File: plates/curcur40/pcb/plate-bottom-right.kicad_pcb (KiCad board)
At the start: 2 copper layers, 116.1 x 88.3 mm, 0 parts

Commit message: move trackball
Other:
- board size 116.1 x 88.3 mm -> 125.6 x 88.3 mm
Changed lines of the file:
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@@
   )
   (net 0 "")
-  (gr_arc (start 119.970400 40.381250) (mid 119.677507 41.088357) (end 118.970400 41.381250) (stroke (width 0.2) (type solid)) (layer "Edge.Cuts"))
-  (gr_line (start 118.970400 41.381250) (end 82.862500 41.381250) (stroke (width 0.2) (type solid)) (layer "Edge.Cuts"))
-  (gr_line (start 82.862500 41.381250) (end 82.862500 62.562500) (stroke (width 0.2) (type solid)) (layer "Edge.Cuts"))
-  (gr_arc (start 82.862500 62.562500) (mid 82.569607 63.269607) (end 81.862500 63.562500) (stroke (width 0.2) (type solid)) (layer "Edge.Cuts"))
-  (gr_line (start 81.862500 63.562500) (end 4.862500 63.562500) (stroke (width 0.2) (type solid)) (layer "Edge.Cuts"))
-  (gr_arc (start 4.862500 63.562500) (mid 4.155393 63.269607) (end 3.862500 62.562500) (stroke (width 0.2) (type solid)) (layer "Edge.Cuts"))
-  (gr_line (start 3.862500 62.562500) (end 3.862500 -16.568750) (stroke (width 0.2) (type solid)) (layer "Edge.Cuts"))
   (gr_arc (start 3.862500 -16.568750) (mid 4.155393 -17.275857) (end 4.862500 -17.568750) (stroke (width 0.2) (type solid)) (layer "Edge.Cuts"))
   (gr_line (start 4.862500 -17.568750) (end 22.928400 -17.568750) (stroke (width 0.2) (type solid)) (layer "Edge.Cuts"))
@@
   (gr_arc (start 118.970400 -17.568750) (mid 119.677507 -17.275857) (end 119.970400 -16.568750) (stroke (width 0.2) (type solid)) (layer "Edge.Cuts"))
   (gr_line (start 119.970400 -16.568750) (end 119.970400 40.381250) (stroke (width 0.2) (type solid)) (layer "Edge.Cuts"))
-  (gr_arc (start 12.450000 44.487500) (mid 12.742893 43.780393) (end 13.450000 43.487500) (stroke (width 0.2) (type solid)) (layer "Edge.Cuts"))
-  (gr_line (start 13.450000 43.487500) (end 20.650000 43.487500) (stroke (width 0.2) (type solid)) (layer "Edge.Cuts"))
-  (gr_arc (start 20.650000 43.487500) (mid 21.357107 43.780393) (end 21.650000 44.487500) (stroke (width 0.2) (type solid)) (layer "Edge.Cuts"))
-  (gr_line (start 21.650000 44.487500) (end 21.650000 60.287500) (stroke (width 0.2) (type solid)) (layer "Edge.Cuts"))
-  (gr_arc (start 21.650000 60.287500) (mid 21.357107 60.994607) (end 20.650000 61.287500) (stroke (width 0.2) (type solid)) (layer "Edge.Cuts"))
-  (gr_line (start 20.650000 61.287500) (end 13.450000 61.287500) (stroke (width 0.2) (type solid)) (layer "Edge.Cuts"))
-  (gr_arc (start 13.450000 61.287500) (mid 12.742893 60.994607) (end 12.450000 60.287500) (stroke (width 0.2) (type solid)) (layer "Edge.Cuts"))
-  (gr_line (start 12.450000 60.287500) (end 12.450000 44.487500) (stroke (width 0.2) (type solid)) (layer "Edge.Cuts"))
+  (gr_arc (start 119.970400 40.381250) (mid 119.677507 41.088357) (end 118.970400 41.381250) (stroke (width 0.2) (type solid)) (layer "Edge.Cuts"))
+  (gr_line (start 118.970400 41.381250) (end 82.862500 41.381250) (stroke (width 0.2) (type solid)) (layer "Edge.Cuts"))
+  (gr_line (start 82.862500 41.381250) (end 82.862500 62.562500) (stroke (width 0.2) (type solid)) (layer "Edge.Cuts"))
+  (gr_arc (start 82.862500 62.562500) (mid 82.569607 63.269607) (end 81.862500 63.562500) (stroke (width 0.2) (type solid)) (layer "Edge.Cuts"))
+  (gr_line (start 81.862500 63.562500) (end -4.662500 63.562500) (stroke (width 0.2) (type solid)) (layer "Edge.Cuts"))
+  (gr_arc (start -4.662500 63.562500) (mid -5.369607 63.269607) (end -5.662500 62.562500) (stroke (width 0.2) (type solid)) (layer "Edge.Cuts"))
+  (gr_line (start -5.662500 62.562500) (end -5.662500 38.400000) (stroke (width 0.2) (type solid)) (layer "Edge.Cuts"))
+  (gr_arc (start -5.662500 38.400000) (mid -5.369607 37.692893) (end -4.662500 37.400000) (stroke (width 0.2) (type solid)) (layer "Edge.Cuts"))
+  (gr_line (start -4.662500 37.400000) (end 3.862500 37.400000) (stroke (width 0.2) (type solid)) (layer "Edge.Cuts"))
+  (gr_line (start 3.862500 37.400000) (end 3.862500 -16.568750) (stroke (width 0.2) (type solid)) (layer "Edge.Cuts"))
+  (gr_arc (start 2.925000 44.487500) (mid 3.217893 43.780393) (end 3.925000 43.487500) (stroke (width 0.2) (type solid)) (layer "Edge.Cuts"))
+  (gr_line (start 3.925000 43.487500) (end 11.125000 43.487500) (stroke (width 0.2) (type solid)) (layer "Edge.Cuts"))
+  (gr_arc (start 11.125000 43.487500) (mid 11.832107 43.780393) (end 12.125000 44.487500) (stroke (width 0.2) (type solid)) (layer "Edge.Cuts"))
+  (gr_line (start 12.125000 44.487500) (end 12.125000 60.287500) (stroke (width 0.2) (type solid)) (layer "Edge.Cuts"))
+  (gr_arc (start 12.125000 60.287500) (mid 11.832107 60.994607) (end 11.125000 61.287500) (stroke (width 0.2) (type solid)) (layer "Edge.Cuts"))
+  (gr_line (start 11.125000 61.287500) (end 3.925000 61.287500) (stroke (width 0.2) (type solid)) (layer "Edge.Cuts"))
+  (gr_arc (start 3.925000 61.287500) (mid 3.217893 60.994607) (end 2.925000 60.287500) (stroke (width 0.2) (type solid)) (layer "Edge.Cuts"))
+  (gr_line (start 2.925000 60.287500) (end 2.925000 44.487500) (stroke (width 0.2) (type solid)) (layer "Edge.Cuts"))
   (gr_circle (center 101.917500 2.381250) (end 103.017500 2.381250) (stroke (width 0.2) (type solid)) (fill none) (layer "Edge.Cuts"))
   (gr_circle (center 101.917500 21.431250) (end 103.017500 21.431250) (stroke (width 0.2) (type solid)) (fill none) (layer "Edge.Cuts"))
   (gr_circle (center 42.862500 -1.190625) (end 43.962500 -1.190625) (stroke (width 0.2) (type solid)) (fill none) (layer "Edge.Cuts"))
   (gr_circle (center 42.862500 38.100000) (end 43.962500 38.100000) (stroke (width 0.2) (type solid)) (fill none) (layer "Edge.Cuts"))
-  (gr_circle (center 8.300000 39.395500) (end 9.400000 39.395500) (stroke (width 0.2) (type solid)) (fill none) (layer "Edge.Cuts"))
-  (gr_circle (center 25.800000 39.395500) (end 26.900000 39.395500) (stroke (width 0.2) (type solid)) (fill none) (layer "Edge.Cuts"))
+  (gr_circle (center -1.225000 39.395500) (end -0.125000 39.395500) (stroke (width 0.2) (type solid)) (fill none) (layer "Edge.Cuts"))
+  (gr_circle (center 16.275000 39.395500) (end 17.375000 39.395500) (stroke (width 0.2) (type solid)) (fill none) (layer "Edge.Cuts"))
 )

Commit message: fail
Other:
- outline, holes or cut-outs redrawn
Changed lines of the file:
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@@
   (gr_line (start 81.862500 63.562500) (end -4.662500 63.562500) (stroke (width 0.2) (type solid)) (layer "Edge.Cuts"))
   (gr_arc (start -4.662500 63.562500) (mid -5.369607 63.269607) (end -5.662500 62.562500) (stroke (width 0.2) (type solid)) (layer "Edge.Cuts"))
-  (gr_line (start -5.662500 62.562500) (end -5.662500 38.400000) (stroke (width 0.2) (type solid)) (layer "Edge.Cuts"))
-  (gr_arc (start -5.662500 38.400000) (mid -5.369607 37.692893) (end -4.662500 37.400000) (stroke (width 0.2) (type solid)) (layer "Edge.Cuts"))
-  (gr_line (start -4.662500 37.400000) (end 3.862500 37.400000) (stroke (width 0.2) (type solid)) (layer "Edge.Cuts"))
-  (gr_line (start 3.862500 37.400000) (end 3.862500 -16.568750) (stroke (width 0.2) (type solid)) (layer "Edge.Cuts"))
-  (gr_arc (start 2.925000 44.487500) (mid 3.217893 43.780393) (end 3.925000 43.487500) (stroke (width 0.2) (type solid)) (layer "Edge.Cuts"))
-  (gr_line (start 3.925000 43.487500) (end 11.125000 43.487500) (stroke (width 0.2) (type solid)) (layer "Edge.Cuts"))
-  (gr_arc (start 11.125000 43.487500) (mid 11.832107 43.780393) (end 12.125000 44.487500) (stroke (width 0.2) (type solid)) (layer "Edge.Cuts"))
-  (gr_line (start 12.125000 44.487500) (end 12.125000 60.287500) (stroke (width 0.2) (type solid)) (layer "Edge.Cuts"))
-  (gr_arc (start 12.125000 60.287500) (mid 11.832107 60.994607) (end 11.125000 61.287500) (stroke (width 0.2) (type solid)) (layer "Edge.Cuts"))
-  (gr_line (start 11.125000 61.287500) (end 3.925000 61.287500) (stroke (width 0.2) (type solid)) (layer "Edge.Cuts"))
-  (gr_arc (start 3.925000 61.287500) (mid 3.217893 60.994607) (end 2.925000 60.287500) (stroke (width 0.2) (type solid)) (layer "Edge.Cuts"))
-  (gr_line (start 2.925000 60.287500) (end 2.925000 44.487500) (stroke (width 0.2) (type solid)) (layer "Edge.Cuts"))
+  (gr_line (start -5.662500 62.562500) (end -5.662500 45.600000) (stroke (width 0.2) (type solid)) (layer "Edge.Cuts"))
+  (gr_arc (start -5.662500 45.600000) (mid -5.369607 44.892893) (end -4.662500 44.600000) (stroke (width 0.2) (type solid)) (layer "Edge.Cuts"))
+  (gr_line (start -4.662500 44.600000) (end 3.862500 44.600000) (stroke (width 0.2) (type solid)) (layer "Edge.Cuts"))
+  (gr_line (start 3.862500 44.600000) (end 3.862500 -16.568750) (stroke (width 0.2) (type solid)) (layer "Edge.Cuts"))
+  (gr_arc (start 3.925000 48.587500) (mid 4.217893 47.880393) (end 4.925000 47.587500) (stroke (width 0.2) (type solid)) (layer "Edge.Cuts"))
+  (gr_line (start 4.925000 47.587500) (end 10.125000 47.587500) (stroke (width 0.2) (type solid)) (layer "Edge.Cuts"))
+  (gr_arc (start 10.125000 47.587500) (mid 10.832107 47.880393) (end 11.125000 48.587500) (stroke (width 0.2) (type solid)) (layer "Edge.Cuts"))
+  (gr_line (start 11.125000 48.587500) (end 11.125000 56.187500) (stroke (width 0.2) (type solid)) (layer "Edge.Cuts"))
+  (gr_arc (start 11.125000 56.187500) (mid 10.832107 56.894607) (end 10.125000 57.187500) (stroke (width 0.2) (type solid)) (layer "Edge.Cuts"))
+  (gr_line (start 10.125000 57.187500) (end 4.925000 57.187500) (stroke (width 0.2) (type solid)) (layer "Edge.Cuts"))
+  (gr_arc (start 4.925000 57.187500) (mid 4.217893 56.894607) (end 3.925000 56.187500) (stroke (width 0.2) (type solid)) (layer "Edge.Cuts"))
+  (gr_line (start 3.925000 56.187500) (end 3.925000 48.587500) (stroke (width 0.2) (type solid)) (layer "Edge.Cuts"))
   (gr_circle (center 101.917500 2.381250) (end 103.017500 2.381250) (stroke (width 0.2) (type solid)) (fill none) (layer "Edge.Cuts"))
   (gr_circle (center 101.917500 21.431250) (end 103.017500 21.431250) (stroke (width 0.2) (type solid)) (fill none) (layer "Edge.Cuts"))
   (gr_circle (center 42.862500 -1.190625) (end 43.962500 -1.190625) (stroke (width 0.2) (type solid)) (fill none) (layer "Edge.Cuts"))
   (gr_circle (center 42.862500 38.100000) (end 43.962500 38.100000) (stroke (width 0.2) (type solid)) (fill none) (layer "Edge.Cuts"))
-  (gr_circle (center -1.225000 39.395500) (end -0.125000 39.395500) (stroke (width 0.2) (type solid)) (fill none) (layer "Edge.Cuts"))
-  (gr_circle (center 16.275000 39.395500) (end 17.375000 39.395500) (stroke (width 0.2) (type solid)) (fill none) (layer "Edge.Cuts"))
+  (gr_circle (center 16.275000 40.387500) (end 17.375000 40.387500) (stroke (width 0.2) (type solid)) (fill none) (layer "Edge.Cuts"))
+  (gr_circle (center 20.525000 58.887500) (end 21.625000 58.887500) (stroke (width 0.2) (type solid)) (fill none) (layer "Edge.Cuts"))
 )

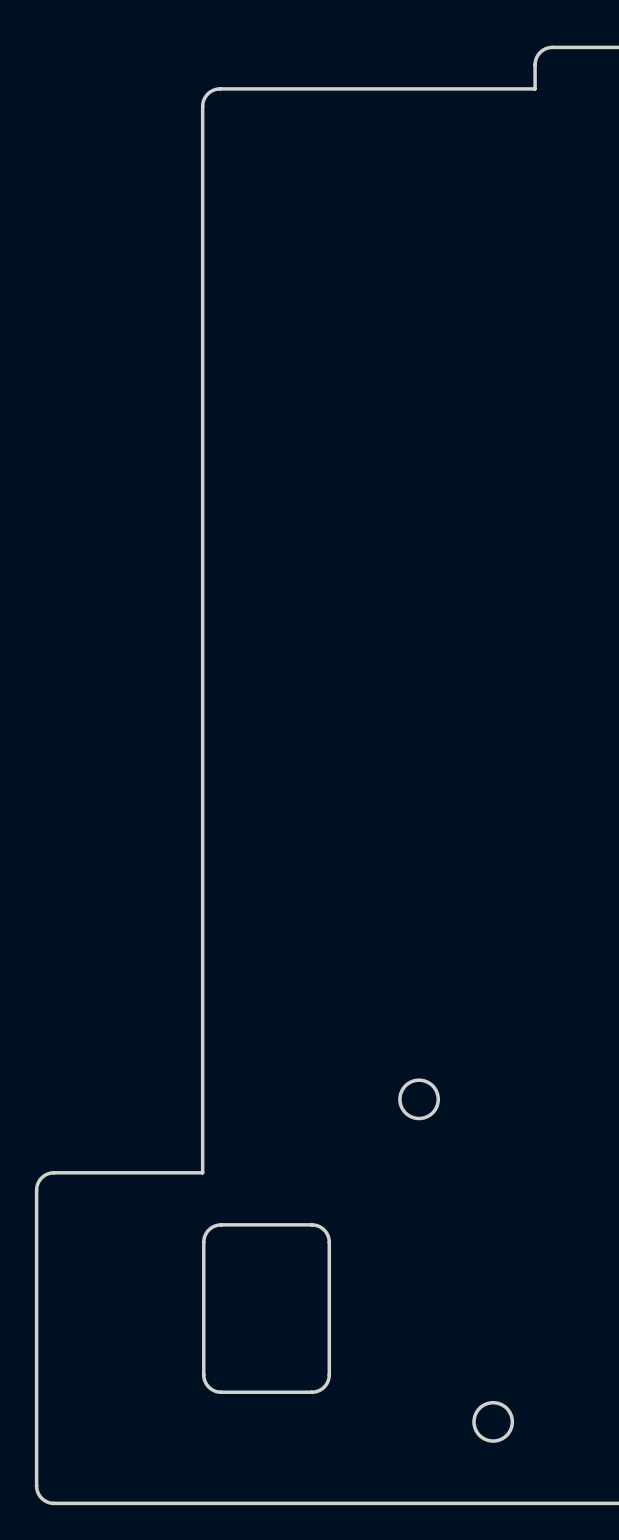
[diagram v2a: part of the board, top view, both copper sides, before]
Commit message: Revert "fail"
This reverts commit f8bb31090bfefcb8a86d31faa946f47e5456d5b7.
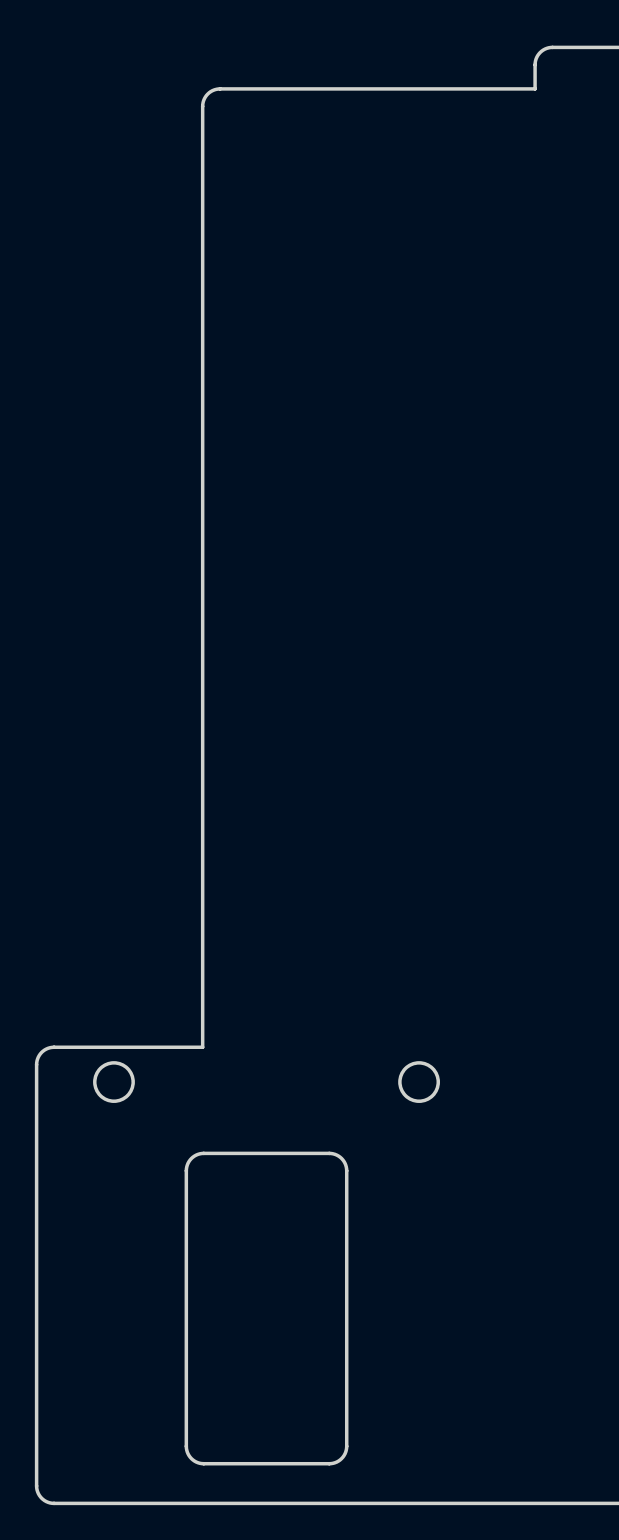
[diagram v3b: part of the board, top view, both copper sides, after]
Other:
- outline, holes or cut-outs redrawn
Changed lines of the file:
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@@
   (gr_line (start 81.862500 63.562500) (end -4.662500 63.562500) (stroke (width 0.2) (type solid)) (layer "Edge.Cuts"))
   (gr_arc (start -4.662500 63.562500) (mid -5.369607 63.269607) (end -5.662500 62.562500) (stroke (width 0.2) (type solid)) (layer "Edge.Cuts"))
-  (gr_line (start -5.662500 62.562500) (end -5.662500 45.600000) (stroke (width 0.2) (type solid)) (layer "Edge.Cuts"))
-  (gr_arc (start -5.662500 45.600000) (mid -5.369607 44.892893) (end -4.662500 44.600000) (stroke (width 0.2) (type solid)) (layer "Edge.Cuts"))
-  (gr_line (start -4.662500 44.600000) (end 3.862500 44.600000) (stroke (width 0.2) (type solid)) (layer "Edge.Cuts"))
-  (gr_line (start 3.862500 44.600000) (end 3.862500 -16.568750) (stroke (width 0.2) (type solid)) (layer "Edge.Cuts"))
-  (gr_arc (start 3.925000 48.587500) (mid 4.217893 47.880393) (end 4.925000 47.587500) (stroke (width 0.2) (type solid)) (layer "Edge.Cuts"))
-  (gr_line (start 4.925000 47.587500) (end 10.125000 47.587500) (stroke (width 0.2) (type solid)) (layer "Edge.Cuts"))
-  (gr_arc (start 10.125000 47.587500) (mid 10.832107 47.880393) (end 11.125000 48.587500) (stroke (width 0.2) (type solid)) (layer "Edge.Cuts"))
-  (gr_line (start 11.125000 48.587500) (end 11.125000 56.187500) (stroke (width 0.2) (type solid)) (layer "Edge.Cuts"))
-  (gr_arc (start 11.125000 56.187500) (mid 10.832107 56.894607) (end 10.125000 57.187500) (stroke (width 0.2) (type solid)) (layer "Edge.Cuts"))
-  (gr_line (start 10.125000 57.187500) (end 4.925000 57.187500) (stroke (width 0.2) (type solid)) (layer "Edge.Cuts"))
-  (gr_arc (start 4.925000 57.187500) (mid 4.217893 56.894607) (end 3.925000 56.187500) (stroke (width 0.2) (type solid)) (layer "Edge.Cuts"))
-  (gr_line (start 3.925000 56.187500) (end 3.925000 48.587500) (stroke (width 0.2) (type solid)) (layer "Edge.Cuts"))
+  (gr_line (start -5.662500 62.562500) (end -5.662500 38.400000) (stroke (width 0.2) (type solid)) (layer "Edge.Cuts"))
+  (gr_arc (start -5.662500 38.400000) (mid -5.369607 37.692893) (end -4.662500 37.400000) (stroke (width 0.2) (type solid)) (layer "Edge.Cuts"))
+  (gr_line (start -4.662500 37.400000) (end 3.862500 37.400000) (stroke (width 0.2) (type solid)) (layer "Edge.Cuts"))
+  (gr_line (start 3.862500 37.400000) (end 3.862500 -16.568750) (stroke (width 0.2) (type solid)) (layer "Edge.Cuts"))
+  (gr_arc (start 2.925000 44.487500) (mid 3.217893 43.780393) (end 3.925000 43.487500) (stroke (width 0.2) (type solid)) (layer "Edge.Cuts"))
+  (gr_line (start 3.925000 43.487500) (end 11.125000 43.487500) (stroke (width 0.2) (type solid)) (layer "Edge.Cuts"))
+  (gr_arc (start 11.125000 43.487500) (mid 11.832107 43.780393) (end 12.125000 44.487500) (stroke (width 0.2) (type solid)) (layer "Edge.Cuts"))
+  (gr_line (start 12.125000 44.487500) (end 12.125000 60.287500) (stroke (width 0.2) (type solid)) (layer "Edge.Cuts"))
+  (gr_arc (start 12.125000 60.287500) (mid 11.832107 60.994607) (end 11.125000 61.287500) (stroke (width 0.2) (type solid)) (layer "Edge.Cuts"))
+  (gr_line (start 11.125000 61.287500) (end 3.925000 61.287500) (stroke (width 0.2) (type solid)) (layer "Edge.Cuts"))
+  (gr_arc (start 3.925000 61.287500) (mid 3.217893 60.994607) (end 2.925000 60.287500) (stroke (width 0.2) (type solid)) (layer "Edge.Cuts"))
+  (gr_line (start 2.925000 60.287500) (end 2.925000 44.487500) (stroke (width 0.2) (type solid)) (layer "Edge.Cuts"))
   (gr_circle (center 101.917500 2.381250) (end 103.017500 2.381250) (stroke (width 0.2) (type solid)) (fill none) (layer "Edge.Cuts"))
   (gr_circle (center 101.917500 21.431250) (end 103.017500 21.431250) (stroke (width 0.2) (type solid)) (fill none) (layer "Edge.Cuts"))
   (gr_circle (center 42.862500 -1.190625) (end 43.962500 -1.190625) (stroke (width 0.2) (type solid)) (fill none) (layer "Edge.Cuts"))
   (gr_circle (center 42.862500 38.100000) (end 43.962500 38.100000) (stroke (width 0.2) (type solid)) (fill none) (layer "Edge.Cuts"))
-  (gr_circle (center 16.275000 40.387500) (end 17.375000 40.387500) (stroke (width 0.2) (type solid)) (fill none) (layer "Edge.Cuts"))
-  (gr_circle (center 20.525000 58.887500) (end 21.625000 58.887500) (stroke (width 0.2) (type solid)) (fill none) (layer "Edge.Cuts"))
+  (gr_circle (center -1.225000 39.395500) (end -0.125000 39.395500) (stroke (width 0.2) (type solid)) (fill none) (layer "Edge.Cuts"))
+  (gr_circle (center 16.275000 39.395500) (end 17.375000 39.395500) (stroke (width 0.2) (type solid)) (fill none) (layer "Edge.Cuts"))
 )

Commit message: fix all
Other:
- outline, holes or cut-outs redrawn

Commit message: fix all
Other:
- board size 125.6 x 88.3 mm -> 125.1 x 92.6 mm
- rule pad_to_mask_clearance: 0.2 -> 0
